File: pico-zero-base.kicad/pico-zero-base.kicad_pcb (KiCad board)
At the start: 2 copper layers, 65 x 30 mm, 6 parts, among them J1 GPIO, U1 Pico

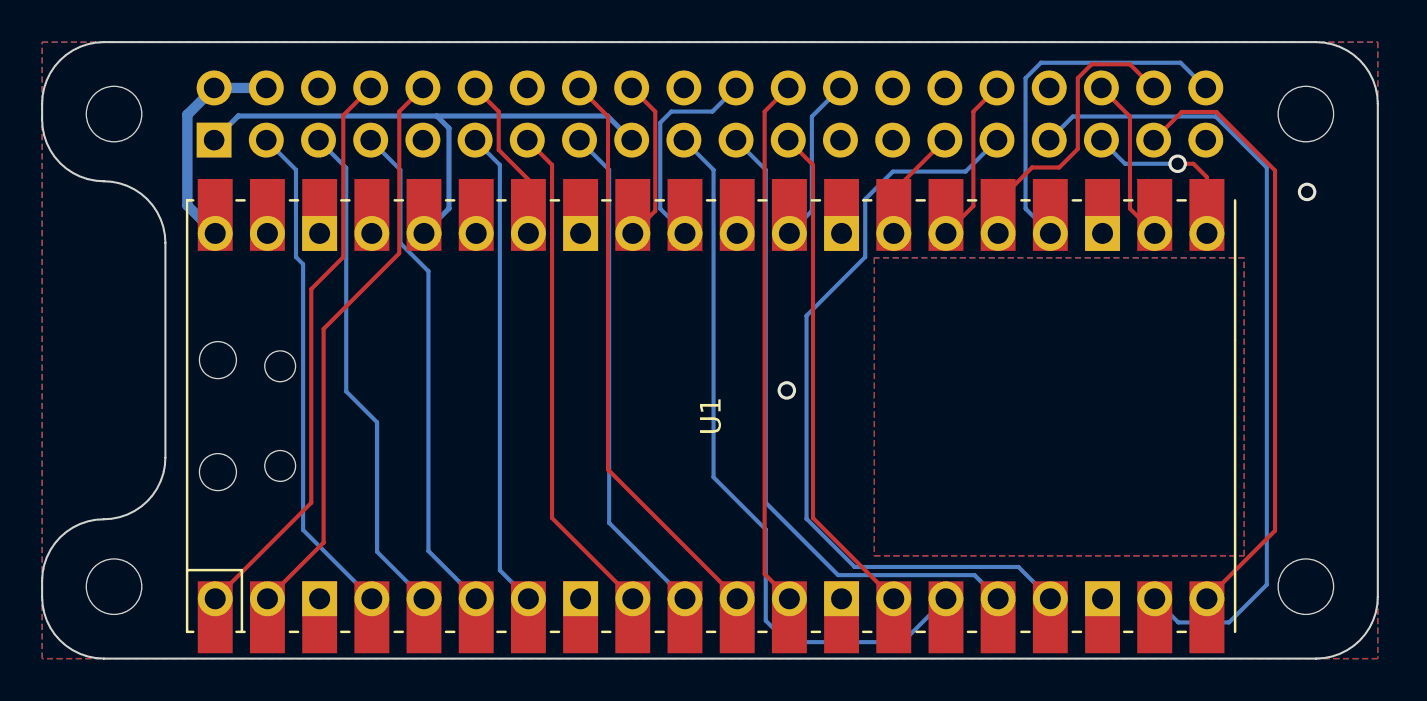
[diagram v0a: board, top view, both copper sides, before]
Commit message: Added reset-button
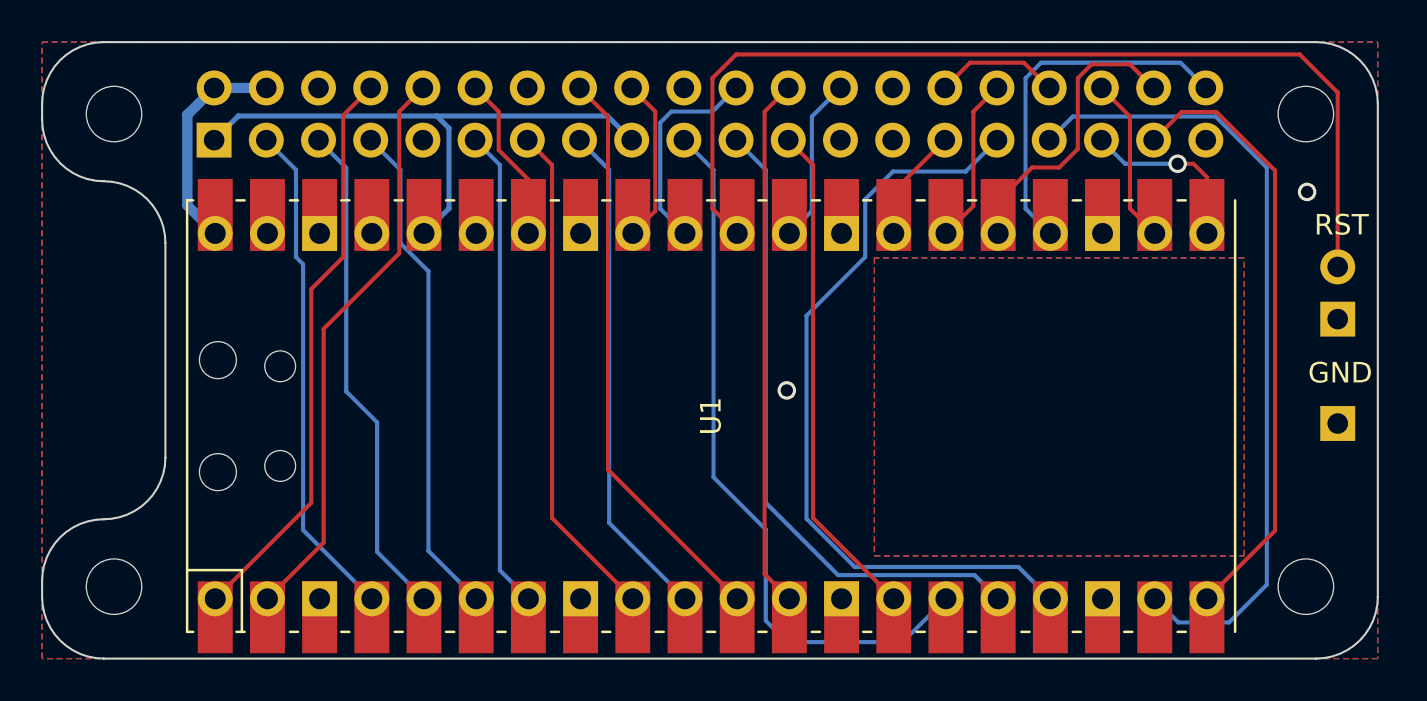
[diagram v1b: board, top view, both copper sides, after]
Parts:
- added SW1: SW_Push_SLIM, user:SW_PUSH_SLIM_1x4, F.Cu at (163.1, 88.6)
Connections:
- U1 pad 30: unconnected-(U1-Pad30) -> /RESET
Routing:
- net /RESET: track 0.00 -> 48.2 mm
- net GND: track 0.00 -> 6.10 mm
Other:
- board text added: "GND"
- board text added: "RST"
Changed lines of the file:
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@@
   (net 30 "+5V")
   (net 31 "+3.3V")
-  (net 32 "unconnected-(U1-Pad30)")
+  (net 32 "/RESET")
   (net 33 "unconnected-(U1-Pad33)")
   (net 34 "unconnected-(U1-Pad35)")
@@
       (net 19 "/GPIO[7]{slash}SPI0.CE1") (pinfunction "GPIO22") (pintype "bidirectional"))
     (pad "30" thru_hole oval (at 8.89 1.27 90) (size 1.7 1.7) (drill 1.02) (layers *.Cu *.Mask)
-      (net 32 "unconnected-(U1-Pad30)") (pinfunction "RUN") (pintype "input+no_connect"))
+      (net 32 "/RESET") (pinfunction "RUN") (pintype "input"))
     (pad "30" smd rect (at 8.89 1.27 90) (size 3.5 1.7) (drill (offset 0.9 0)) (layers "F.Cu" "F.Mask")
-      (net 32 "unconnected-(U1-Pad30)") (pinfunction "RUN") (pintype "input+no_connect"))
+      (net 32 "/RESET") (pinfunction "RUN") (pintype "input"))
     (pad "31" smd rect (at 8.89 -1.27 90) (size 3.5 1.7) (drill (offset 0.9 0)) (layers "F.Cu" "F.Mask")
       (net 16 "/GPIO[25]") (pinfunction "GPIO26_ADC0") (pintype "bidirectional"))
@@
     (fp_circle (center 0 0) (end 2.95 0) (layer "F.CrtYd") (width 0.05) (fill none))
     (pad "" np_thru_hole circle locked (at 0 0) (size 2.7 2.7) (drill 2.7) (layers *.Cu *.Mask))
+  )
+  (footprint "user:SW_PUSH_SLIM_1x4" (layer "F.Cu")
+    (at 163.05 88.56 90)
+    (descr "Slim Pushbutton")
+    (tags "connector")
+    (property "Sheetfile" "pico-zero-base.kicad_sch")
+    (property "Sheetname" "")
+    (attr exclude_from_pos_files)
+    (fp_text reference "SW1" (at 1.27 -3.175 90) (layer "F.SilkS") hide
+      (effects (font (size 1 1) (thickness 0.15)))
+    )
+    (fp_text value "SW_Push_SLIM" (at 3.73126 2.92608 90) (layer "F.Fab") hide
+      (effects (font (size 1 1) (thickness 0.15)))
+    )
+    (fp_text user "${REFERENCE}" (at 1.27 1.27 90) (layer "F.Fab") hide
+      (effects (font (size 1 1) (thickness 0.15)))
+    )
+    (fp_line (start -1.27 -1.8) (end 8.89 -1.8) (layer "F.CrtYd") (width 0.05))
+    (fp_line (start 8.89 -1.8) (end 8.89 1.8) (layer "F.CrtYd") (width 0.05))
+    (fp_line (start -1.27 -1.8) (end -1.27 1.8) (layer "F.CrtYd") (width 0.05))
+    (fp_line (start -1.27 1.8) (end 8.89 1.8) (layer "F.CrtYd") (width 0.05))
+    (pad "1" thru_hole rect (at 5.08 0 90) (size 1.7 1.7) (drill 1) (layers *.Cu *.Mask)
+      (net 1 "GND") (pinfunction "1") (pintype "passive"))
+    (pad "1" thru_hole rect (at 0 0 90) (size 1.7 1.7) (drill 1) (layers *.Cu *.Mask)
+      (net 1 "GND") (pinfunction "1") (pintype "passive"))
+    (pad "2" thru_hole circle (at 7.62 0 90) (size 1.7 1.7) (drill 1) (layers *.Cu *.Mask)
+      (net 32 "/RESET") (pinfunction "2") (pintype "passive"))
   )
   (footprint "MountingHole:MountingHole_2.7mm_M2.5" locked (layer "F.Cu")
@@
   (gr_arc (start 103 76.77) (mid 105.12132 77.64868) (end 106 79.77) (layer "Edge.Cuts") (width 0.1))
   (gr_line (start 162 70) (end 103 70) (layer "Edge.Cuts") (width 0.1))
+  (gr_text "RST" (at 161.9 78.9) (layer "F.SilkS")
+    (effects (font (size 1 1) (thickness 0.15)) (justify left))
+  )
+  (gr_text "GND" (at 161.6 86.1) (layer "F.SilkS")
+    (effects (font (size 1 1) (thickness 0.15)) (justify left))
+  )
+  (segment (start 147.78 71) (end 145.16 71) (width 0.2) (layer "F.Cu") (net 1))
+  (segment (start 145.16 71) (end 143.93 72.23) (width 0.2) (layer "F.Cu") (net 1))
+  (segment (start 149.01 72.23) (end 147.78 71) (width 0.2) (layer "F.Cu") (net 1))
   (via (at 161.56 77.29) (size 0.9) (drill 0.6) (layers "F.Cu" "B.Cu") (free) (net 1))
   (via (at 136.24 86.95) (size 0.9) (drill 0.6) (layers "F.Cu" "B.Cu") (free) (net 1))
@@
   (segment (start 109.545 73.595) (end 119.206701 73.595) (width 0.25) (layer "B.Cu") (net 31))
   (segment (start 127.515 73.595) (end 128.69 74.77) (width 0.25) (layer "B.Cu") (net 31))
+  (segment (start 132.62 78.105) (end 132.62 71.753654) (width 0.2) (layer "F.Cu") (net 32))
+  (segment (start 133.825 79.31) (end 132.62 78.105) (width 0.2) (layer "F.Cu") (net 32))
+  (segment (start 161.2 70.6) (end 163.05 72.45) (width 0.2) (layer "F.Cu") (net 32))
+  (segment (start 133.773654 70.6) (end 161.2 70.6) (width 0.2) (layer "F.Cu") (net 32))
+  (segment (start 163.05 72.45) (end 163.05 80.94) (width 0.2) (layer "F.Cu") (net 32))
+  (segment (start 132.62 71.753654) (end 133.773654 70.6) (width 0.2) (layer "F.Cu") (net 32))
   (zone (net 1) (net_name "GND") (layer "F.Cu") (hatch edge 0.508)
     (connect_pads (clearance 0))

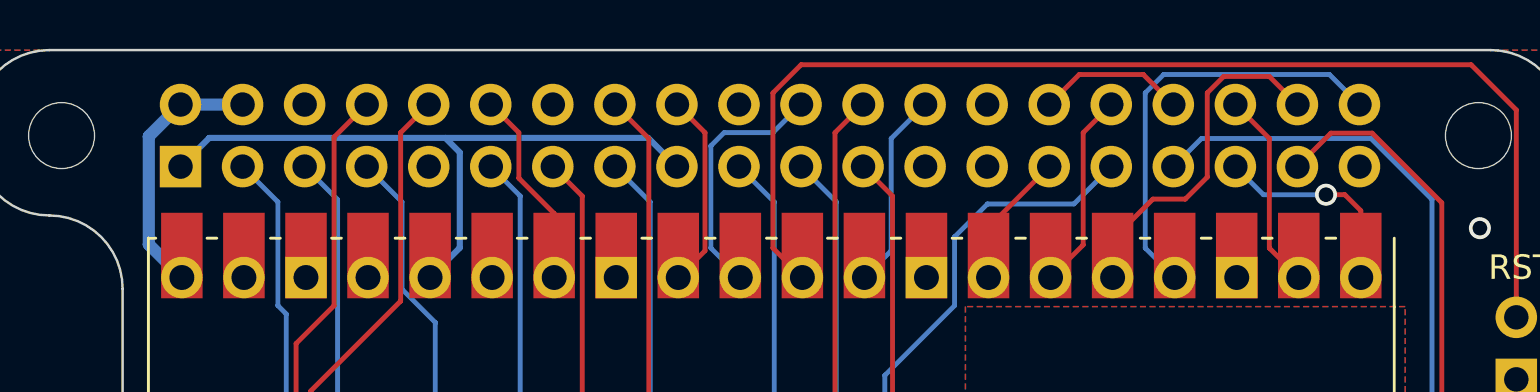
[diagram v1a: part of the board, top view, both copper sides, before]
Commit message: use pin-header instead of socket Rev 1.1
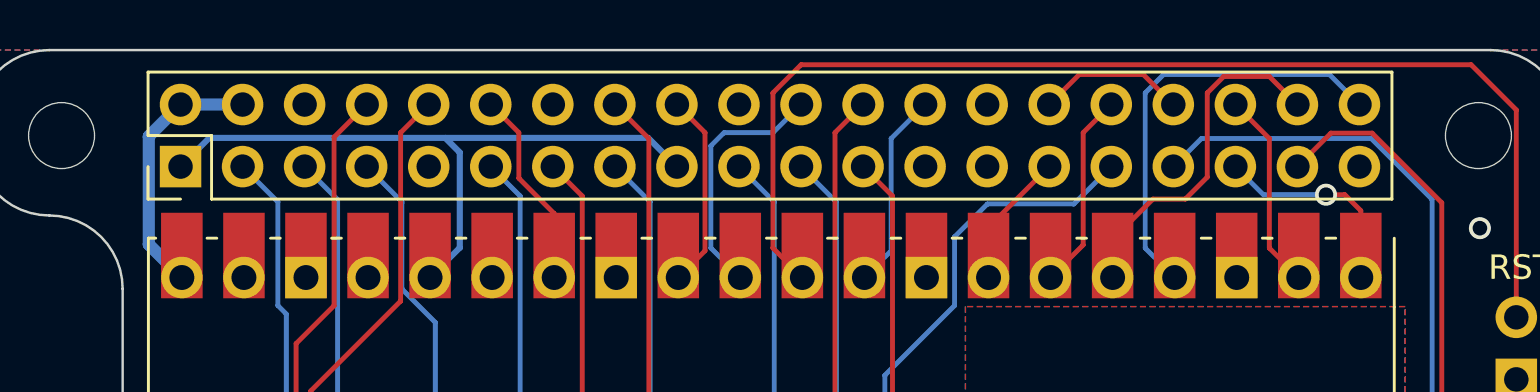
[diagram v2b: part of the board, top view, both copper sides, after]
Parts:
- J1: footprint Connector_PinSocket_2.54mm:PinSocket_2x20_P2.54mm_Vertical -> Connector_PinHeader_2.54mm:PinHeader_2x20_P2.54mm_Vertical; moved to F.Cu
- turned J1 to 90 degrees
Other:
- board text added: "Rev 1.1"
- board text added: "https://github.com/bablokb/pcb-pico-pi-base"
